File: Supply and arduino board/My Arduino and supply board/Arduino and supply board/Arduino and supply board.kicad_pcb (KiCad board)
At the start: 2 copper layers, 44.5 x 57.2 mm, 60 parts, among them J1 USB_C_Receptacle_USB2.0, J2 Conn_01x03, J3 Conn_01x03, J4 Conn_01x03, J5 Conn_01x03, J6 Conn_01x03, J7 Conn_01x03, Q2 16MHz, T1 FDN340V, U1 LM358D, U2 LP2985-3.3, U3 MC33269D-5.0, U4 MC33269ST-5.0T3, U5 TPS629DRL, U7 Atmega328P-PU, U8 FT231XQ, Y2 16MHz

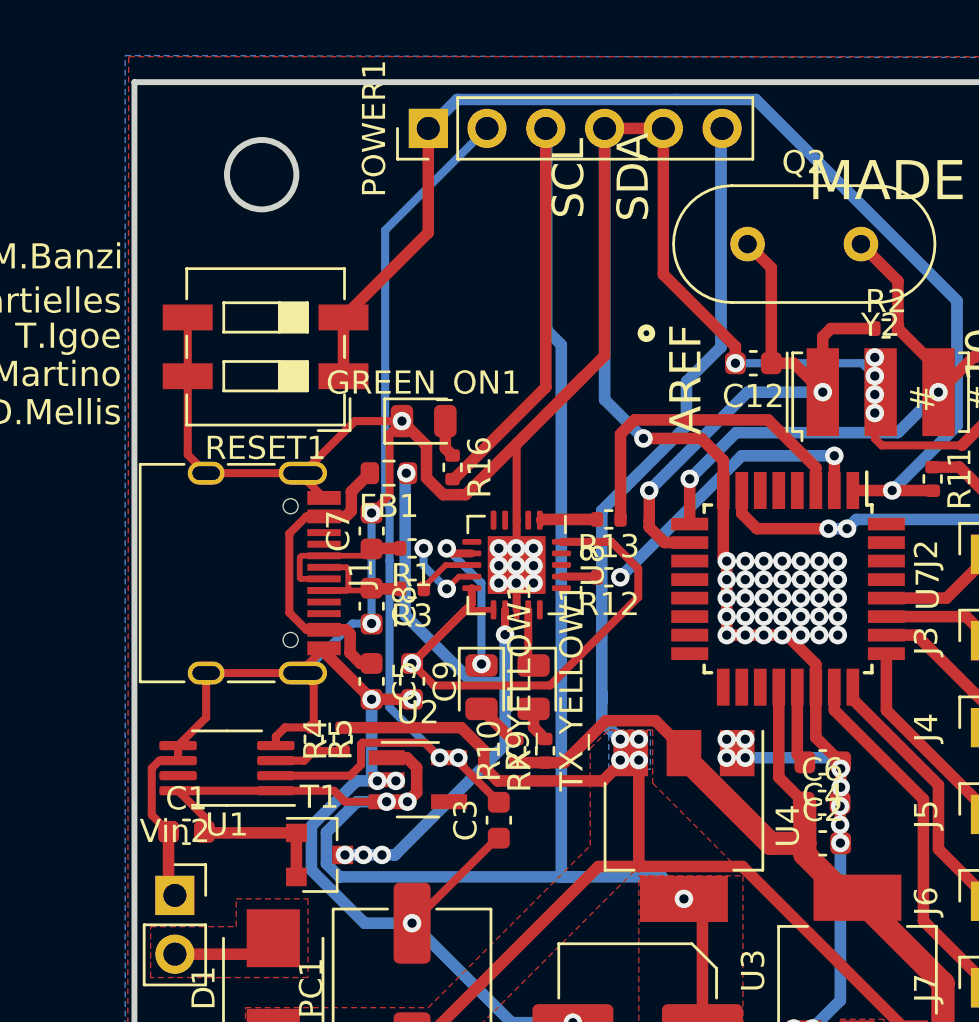
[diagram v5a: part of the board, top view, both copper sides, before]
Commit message: add usb protect
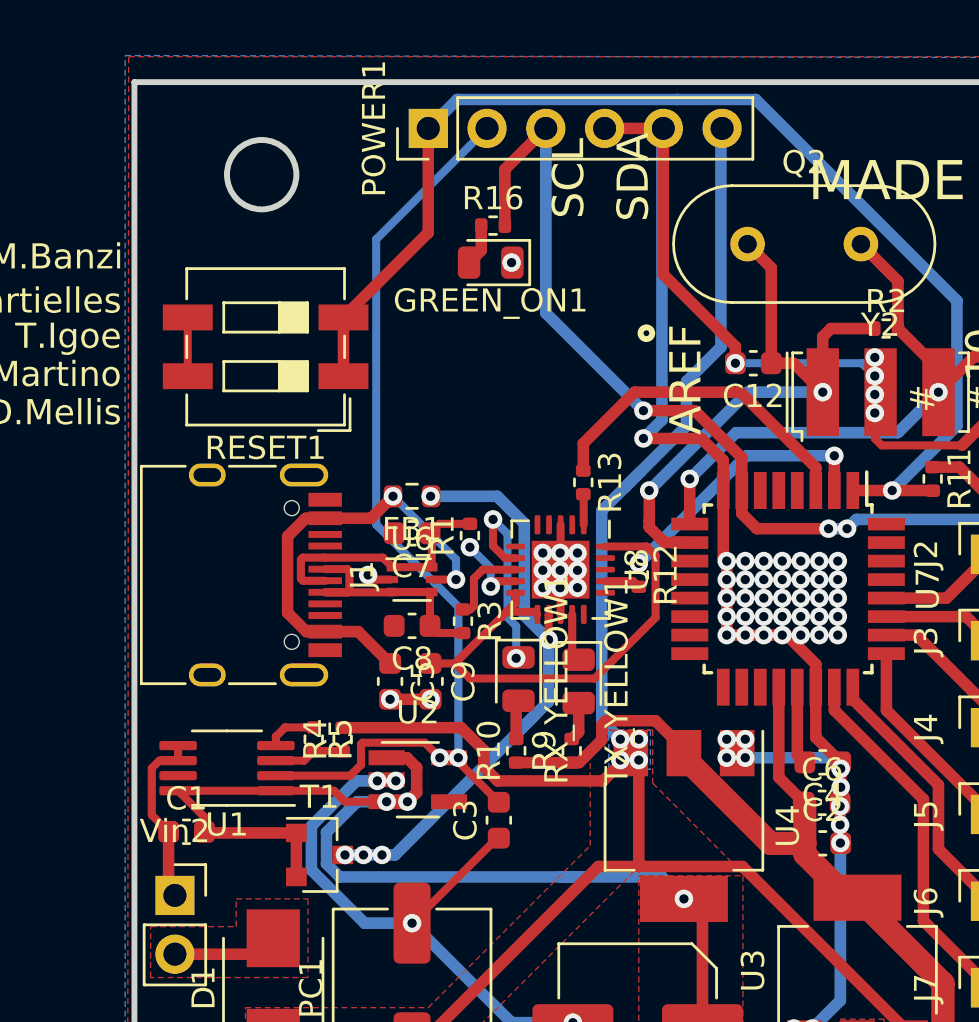
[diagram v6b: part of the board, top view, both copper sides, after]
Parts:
- added U6: USBLC6-2P6, Package_TO_SOT_SMD:SOT-666, F.Cu at (144.2, 61.6)
- moved R16 10.6 mm to (147.7, 46.3), turned to 0 degrees
- moved GREEN_ON1 7.44 mm to (147.6, 47.9), turned to 180 degrees
- moved R3 2.61 mm to (146.4, 63.4), turned to 270 degrees
- moved R1 2.56 mm to (146.7, 59.7), turned to 90 degrees
- moved TX_YELLOW1 1.97 mm to (151.4, 66.0)
- moved C8 1.95 mm to (144.2, 63.6), turned to 180 degrees
- moved R13 1.94 mm to (151.6, 57.4), turned to 270 degrees
- moved U8 1.91 mm to (150.6, 61.1)
- moved C7 1.75 mm to (144.2, 59.6), turned to 180 degrees
- moved RX_YELLOW1 1.64 mm to (148.8, 65.9)
- moved FB1 1.41 mm to (144.2, 58.0)
- moved R12 1.30 mm to (154.0, 61.4), turned to 270 degrees
- moved R9 1.15 mm to (151.1, 69.0)
- moved C5 0.80 mm to (143.2, 66.0)
- moved C9 0.80 mm to (145.0, 66.0)
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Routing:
- net GND: track 266.8 -> 192.6 mm, vias 73 -> 72
- net +5V: track 211.1 -> 187.4 mm, vias 5 -> 6
- net Net-(C5-Pad1): track 13.4 -> 19.6 mm, vias 0 -> 2
- net Net-(C7-Pad1): track 6.46 -> 11.2 mm
- net Net-(C8-Pad1): track 6.36 -> 10.7 mm
- net Net-(C9-Pad1): track 25.6 -> 21.6 mm, vias 1 -> 0
- net /USBVCC: track 26.5 -> 30.2 mm
- net /M8TXD: track 4.89 -> 1.33 mm
- net /RXLED: track 6.79 -> 8.90 mm
- net Net-(R3-Pad1): track 2.55 -> 3.69 mm
- net Net-(R12-Pad1): track 12.9 -> 11.9 mm
- net /+3V3: track 41.9 -> 42.6 mm

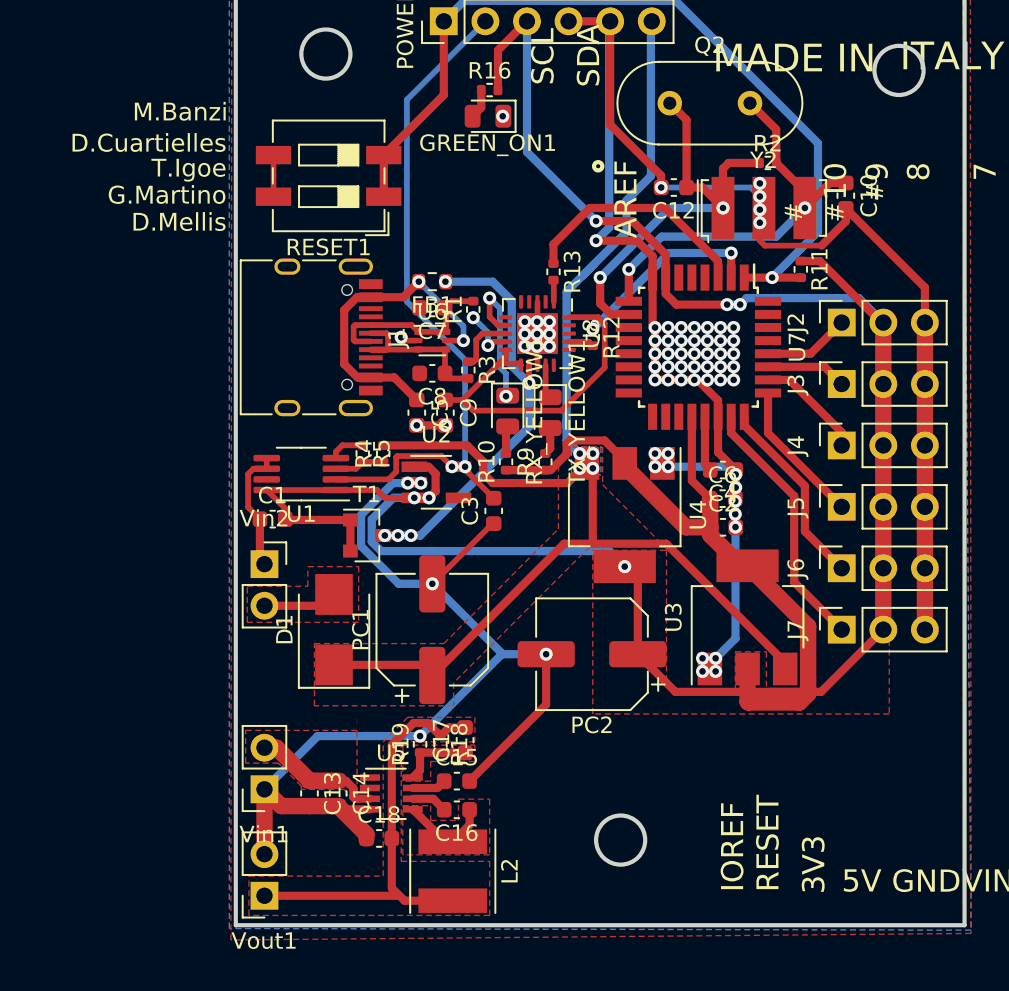
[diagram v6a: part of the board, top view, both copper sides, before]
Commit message: add text on PCB
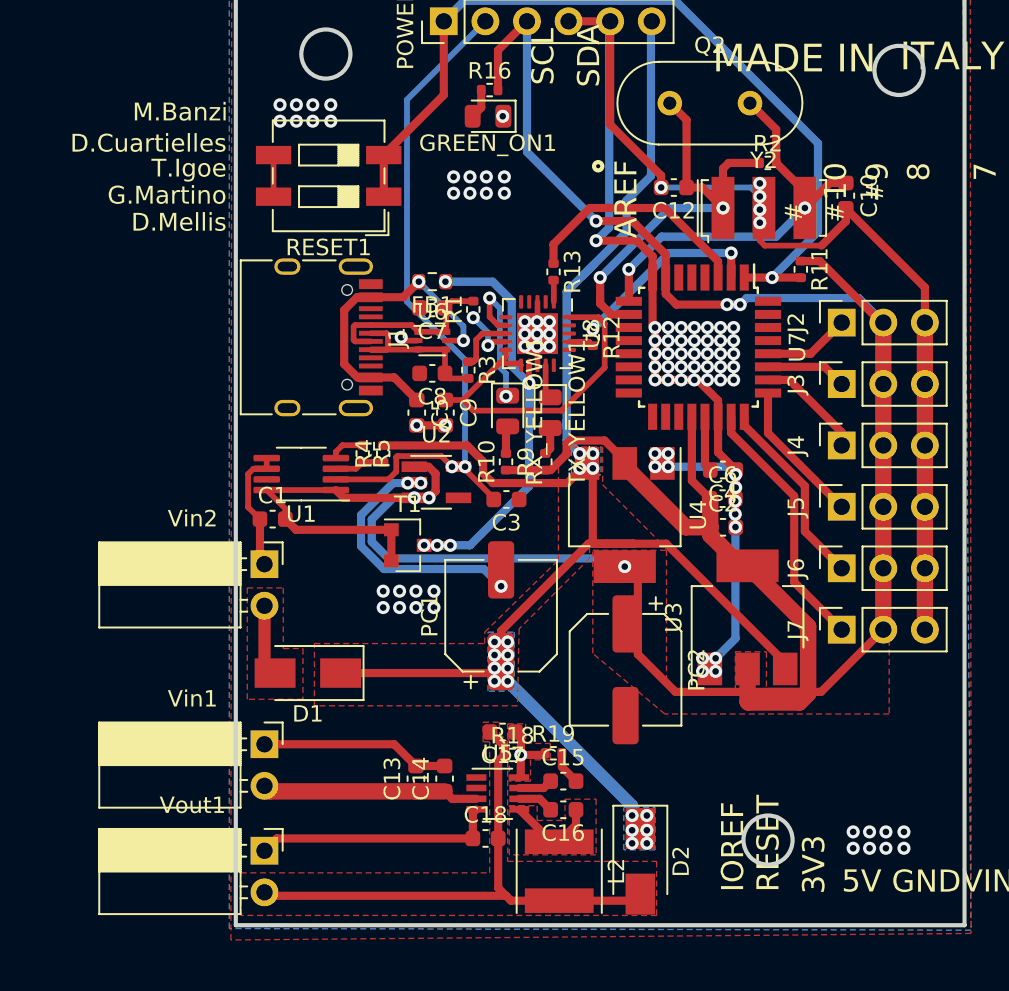
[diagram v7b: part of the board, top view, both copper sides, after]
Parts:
- added D2: 1N4007, Diode_SMD:D_SMA, F.Cu at (156.9, 93.4)
- D1: value M7 -> 1N4007; footprint Diode_SMD:D_SMB -> Diode_SMD:D_SMA
- Vin1, Vin2, Vout1: footprint Connector_PinSocket_2.54mm:PinSocket_1x02_P2.54mm_Vertical -> Connector_PinSocket_2.54mm:PinSocket_1x02_P2.54mm_Horizontal
- moved R19 8.17 mm to (151.6, 86.8), turned to 0 degrees
- moved C13 6.56 mm to (143.2, 88.3), turned to 90 degrees
- moved C14 6.56 mm to (144.9, 88.3), turned to 90 degrees
- moved C15 6.50 mm to (152.2, 88.5)
- moved C16 6.50 mm to (152.2, 90.2)
- moved C18 6.50 mm to (147.4, 92.0)
- moved L2 6.50 mm to (151.9, 94.0)
- moved U5 6.50 mm to (148.2, 89.2)
- moved R18 4.45 mm to (149.1, 86.9), turned to 0 degrees
- moved PC1 4.29 mm to (148.4, 78.4)
- moved D1 3.10 mm to (136.6, 81.9), turned to 180 degrees
- moved Vin1 2.75 mm to (133.9, 86.2), turned to 0 degrees
- moved Vout1 2.75 mm to (133.9, 92.7), turned to 0 degrees
- moved T1 2.57 mm to (142.7, 74.1)
- moved C17 2.35 mm to (148.5, 85.5), turned to 180 degrees
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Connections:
- Vout1 pad 1: Net-(C17-Pad2) -> GND
- Vout1 pad 2: GND -> Net-(C17-Pad2)
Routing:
- net GND: track 192.6 -> 170.1 mm, vias 72 -> 78
- net /VIN: track 84.7 -> 98.9 mm, vias 4 -> 18
- net Net-(C17-Pad2): track 26.6 -> 34.0 mm
- net Net-(C13-Pad1): track 8.03 -> 13.3 mm
- net +5V: track 187.4 -> 189.2 mm
- net /USBVCC: track 30.2 -> 30.7 mm
- net Net-(C17-Pad1): track 4.45 -> 4.47 mm, vias 0 -> 1
- net (no net): vias 0 -> 24
- removed copper zone on F.Cu, net Net-(C13-Pad1)
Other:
- outline, holes or cut-outs redrawn
- board text added: "12Vin"
- board text added: "12Vout"
- board text added: "24Vin"

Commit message: new DC-DC power supply
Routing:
- net GND: vias 78 -> 102
- net (no net): vias 24 -> 0
